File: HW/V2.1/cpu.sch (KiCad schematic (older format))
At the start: 74 parts, among them Q1 FDN360P, Q4 FDN360P, T2 TS-1136EVW, U1 STM32F302-SQ48, U2 MIC5501-3.0V, U3 BY25Q64ASSIG, U5 ESP8266EX, X1 TC2050-IDC, X3 TC2050-IDC

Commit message: updated values
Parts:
- removed F1: 120R@100MHz, Resistor_SMD:R_0805_2012Metric, symbol Device:Ferrite_Bead
- added FB2: Ferret, Inductor_SMD:L_0805_2012Metric, symbol Device:Ferrite_Bead
- C11, C15: value 4u7 16V -> 82n
- C8: value 10u 6,3V -> 1u 25V
- C9: value 22p 50V -> 18p 50V
- FB1: value Ferrite_Bead -> Ferret
- T2: value TS-1136EVW -> Panasonic_EVQPUL_EVQPUC
- U1: value STM32F302-SQ48 -> STM32F334
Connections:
- net 3V3: now also FB2.2
- net at C3.2, C4.2, U1.9 (VDDA/VREF+): now also FB2.1
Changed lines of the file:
@@
 P 9700 1900
 F 0 "C8" V 9803 1690 60  0000 R CNN
-F 1 "10u 6,3V" V 9697 1690 60  0000 R CNN
+F 1 "1u 25V" V 9697 1690 60  0000 R CNN
 F 2 "Capacitor_SMD:C_0603_1608Metric" H 9610 1710 60  0001 C CNN
 F 3 "" H 9610 1710 60  0000 C CNN
@@
 P 1950 7100
 F 0 "C15" H 2000 6837 60  0000 C CNN
-F 1 "4u7 16V" H 2000 6731 60  0000 C CNN
+F 1 "82n" H 2000 6731 60  0000 C CNN
 F 2 "Capacitor_SMD:C_0603_1608Metric" H 1940 6810 60  0001 C CNN
 F 3 "" H 1940 6810 60  0000 C CNN
@@
 P 1950 6700
 F 0 "C11" H 2000 6869 60  0000 C CNN
-F 1 "4u7 16V" H 2000 6763 60  0000 C CNN
+F 1 "82n" H 2000 6763 60  0000 C CNN
 F 2 "Capacitor_SMD:C_0603_1608Metric" H 1940 6410 60  0001 C CNN
 F 3 "" H 1940 6410 60  0000 C CNN
@@
 P 12750 4950
 F 0 "C9" H 12800 5119 60  0000 C CNN
-F 1 "22p 50V" H 12800 5013 60  0000 C CNN
+F 1 "18p 50V" H 12800 5013 60  0000 C CNN
 F 2 "Capacitor_SMD:C_0603_1608Metric" H 12740 4660 60  0001 C CNN
 F 3 "" H 12740 4660 60  0000 C CNN
@@
 P 15450 6100
 F 0 "T2" V 15397 5870 60  0000 R CNN
-F 1 "TS-1136EVW" V 15503 5870 60  0000 R CNN
+F 1 "Panasonic_EVQPUL_EVQPUC" V 15750 5750 60  0000 R CNN
 F 2 "Button_Switch_SMD:Panasonic_EVQPUL_EVQPUC" H 15440 6300 60  0001 C CNN
 F 3 "" H 15440 6300 60  0000 C CNN
@@
 Wire Wire Line
 	9800 1650 9800 1600
-$Comp
-L Device:Ferrite_Bead F1
-U 1 1 5D2B5837
-P 3100 1800
-F 0 "F1" V 2804 1800 60  0000 C CNN
-F 1 "120R@100MHz" V 2910 1800 60  0000 C CNN
-F 2 "Resistor_SMD:R_0805_2012Metric" V 2910 1800 60  0001 C CNN
-F 3 "" H 2700 1500 60  0000 C CNN
-	1    3100 1800
-	0    1    1    0
-$EndComp
 Wire Wire Line
 	2950 1800 2900 1800
@@
 P 4700 3700
 F 0 "U1" H 4700 6489 60  0000 C CNN
-F 1 "STM32F302-SQ48" H 4700 6383 60  0000 C CNN
+F 1 "STM32F334" H 4700 6383 60  0000 C CNN
 F 2 "Package_QFP:TQFP-48_7x7mm_P0.5mm" H 4100 4950 60  0001 C CNN
 F 3 "" H 4100 4950 60  0000 C CNN
@@
 P 7900 8600
 F 0 "FB1" H 8037 8646 50  0000 L CNN
-F 1 "Ferrite_Bead" H 8037 8555 50  0000 L CNN
+F 1 "Ferret" H 8037 8555 50  0000 L CNN
 F 2 "Inductor_SMD:L_0805_2012Metric" V 7830 8600 50  0001 C CNN
 F 3 "~" H 7900 8600 50  0001 C CNN
@@
 Connection ~ 7900 9400
 NoConn ~ 11450 5050
+$Comp
+L Device:Ferrite_Bead FB2
+U 1 1 5D49F431
+P 3100 1800
+F 0 "FB2" V 2826 1800 50  0000 C CNN
+F 1 "Ferret" V 2917 1800 50  0000 C CNN
+F 2 "Inductor_SMD:L_0805_2012Metric" V 3030 1800 50  0001 C CNN
+F 3 "~" H 3100 1800 50  0001 C CNN
+	1    3100 1800
+	0    1    1    0
+$EndComp
 $EndSCHEMATC

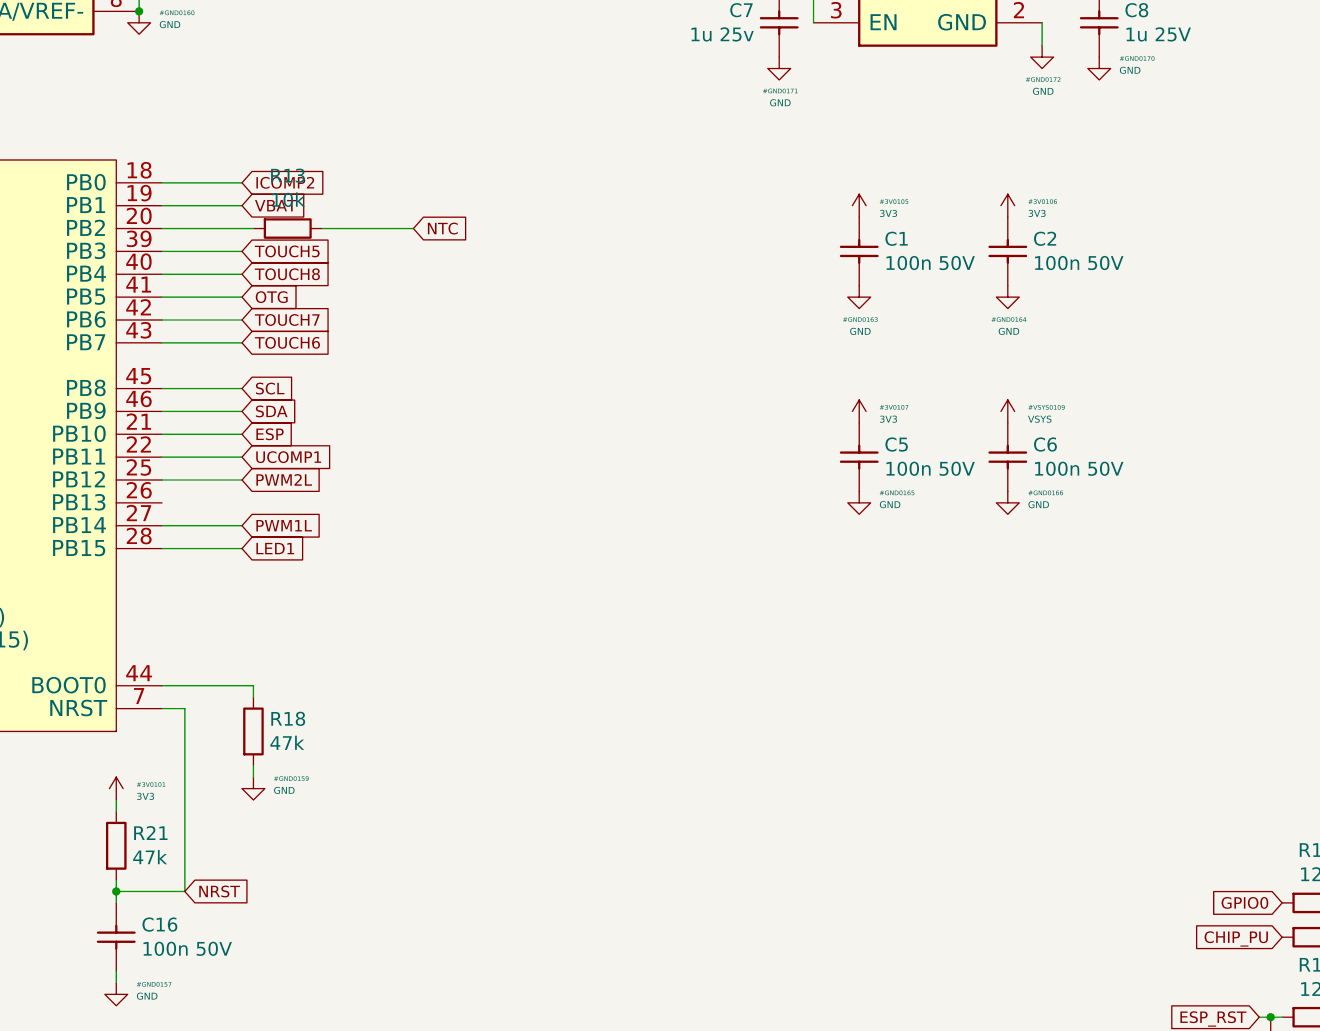
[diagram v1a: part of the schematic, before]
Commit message: added touch ic, fixed sk6812
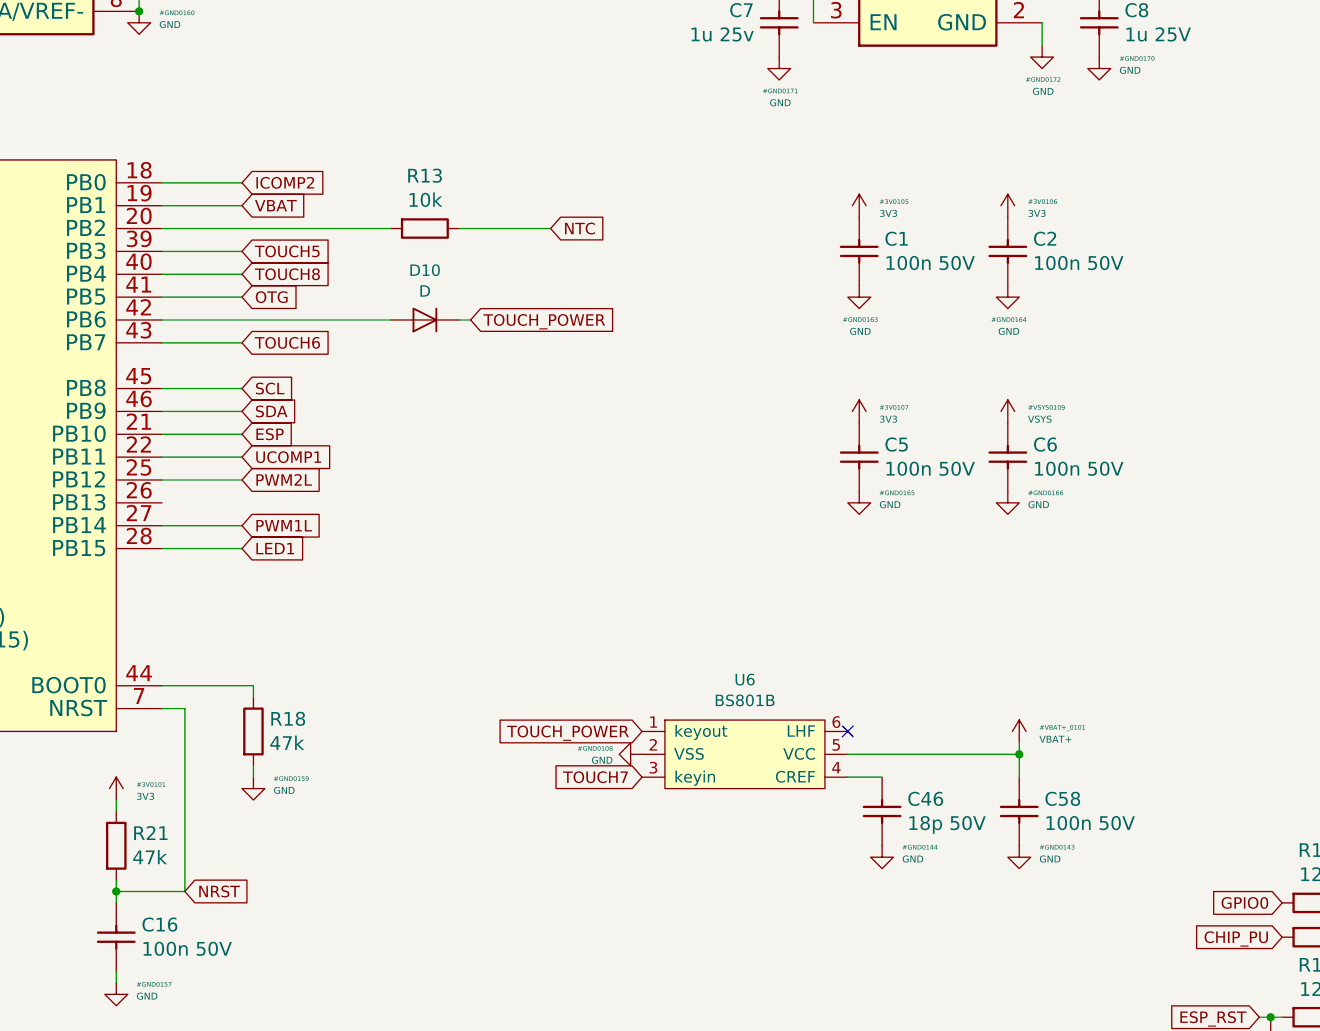
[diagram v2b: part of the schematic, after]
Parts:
- added C46: 18p 50V, Capacitor_SMD:C_0603_1608Metric, symbol EO:C-0402-18p-50V
- added C58: 100n 50V, Capacitor_SMD:C_0603_1608Metric, symbol EO:C-0603-100n-50V
- added D10: D, Diode_SMD:D_SOD-123F, symbol Device:D
- added U6: BS801B, Package_TO_SOT_SMD:SOT-23-6, symbol otter:BS801B
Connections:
- net GND: now also C46.1, C58.2, U6.2 (VSS)
- net TOUCH7: now also U6.3 (keyin); no longer U1.42 (PB6)
- new net: D10.2 (A), U1.42 (PB6)
- new net: C46.2, U6.4 (CREF)
- new net TOUCH_POWER: D10.1 (K), U6.1 (keyout)
- new net VBAT+: C58.1, U6.5 (VCC)
- no-connect marks 1 -> 2
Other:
- moved on the sheet: R13
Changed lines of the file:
@@
 L Device:R R13
 U 1 1 5D2B584B
-P 6250 2750
-F 0 "R13" V 6021 2750 60  0000 C CNN
-F 1 "10k" V 6127 2750 60  0000 C CNN
-F 2 "Resistor_SMD:R_0603_1608Metric" H 6250 2510 60  0001 C CNN
-F 3 "" H 6250 2510 60  0000 C CNN
-	1    6250 2750
+P 6850 2750
+F 0 "R13" V 6621 2750 60  0000 C CNN
+F 1 "10k" V 6727 2750 60  0000 C CNN
+F 2 "Resistor_SMD:R_0603_1608Metric" H 6850 2510 60  0001 C CNN
+F 3 "" H 6850 2510 60  0000 C CNN
+	1    6850 2750
 	0    1    1    0
 $EndComp
@@
 	6100 4800 6100 4750
 Wire Wire Line
-	6400 2750 6800 2750
+	7000 2750 7400 2750
 Connection ~ 8400 1650
 Wire Wire Line
@@
 	5700 2950 6050 2950
 Wire Wire Line
-	5700 3150 6050 3150
-Wire Wire Line
 	5700 3250 6050 3250
 Wire Wire Line
@@
 Wire Wire Line
 	3200 3150 3700 3150
-Wire Wire Line
-	5700 2750 6100 2750
 Wire Wire Line
 	3250 1800 3400 1800
@@
 Text GLabel 5800 5650 2    50   Input ~ 0
 NRST
-Text GLabel 6800 2750 2    50   Input ~ 0
+Text GLabel 7400 2750 2    50   Input ~ 0
 NTC
 Text GLabel 6050 2850 2    50   Input ~ 0
@@
 Text GLabel 6050 3050 2    50   Input ~ 0
 OTG
-Text GLabel 6050 3150 2    50   Input ~ 0
-TOUCH7
 Text GLabel 6050 2950 2    50   Input ~ 0
 TOUCH8
@@
 Text Label 3200 4050 0    60   ~ 0
 SWCLK
-Text GLabel 1350 5800 3    50   Input ~ 0
-NTC
 Text GLabel 1500 7200 0    50   Input ~ 0
 TOUCH5
@@
 	0    1    1    0
 $EndComp
+$Comp
+L otter:BS801B U6
+U 1 1 5D767019
+P 8250 5050
+F 0 "U6" H 8250 5375 50  0000 C CNN
+F 1 "BS801B" H 8250 5284 50  0000 C CNN
+F 2 "Package_TO_SOT_SMD:SOT-23-6" H 8250 5250 50  0001 C CNN
+F 3 "" H 8250 5250 50  0001 C CNN
+	1    8250 5050
+	1    0    0    -1
+$EndComp
+Text GLabel 7800 5150 0    50   Input ~ 0
+TOUCH7
+$Comp
+L power:GND #GND0108
+U 1 1 5D774B01
+P 7800 5050
+F 0 "#GND0108" V 7775 4923 20  0000 R CNN
+F 1 "GND" V 7827 4923 30  0000 R CNN
+F 2 "" H 7800 5050 70  0000 C CNN
+F 3 "" H 7800 5050 70  0000 C CNN
+	1    7800 5050
+	0    1    1    0
+$EndComp
+Text GLabel 7800 4950 0    50   Input ~ 0
+TOUCH_POWER
+NoConn ~ 8700 4950
+$Comp
+L EO:C-0603-100n-50V C58
+U 1 1 5D7A59D1
+P 9550 5250
+F 0 "C58" V 9547 5260 60  0000 L CNN
+F 1 "100n 50V" V 9653 5260 60  0000 L CNN
+F 2 "Capacitor_SMD:C_0603_1608Metric" H 9460 5060 60  0001 C CNN
+F 3 "" H 9460 5060 60  0000 C CNN
+	1    9550 5250
+	0    1    1    0
+$EndComp
+$Comp
+L power:GND #GND0143
+U 1 1 5D7A59D8
+P 9450 5450
+F 0 "#GND0143" H 9538 5443 20  0000 L CNN
+F 1 "GND" H 9538 5391 30  0000 L CNN
+F 2 "" H 9450 5450 70  0000 C CNN
+F 3 "" H 9450 5450 70  0000 C CNN
+	1    9450 5450
+	1    0    0    -1
+$EndComp
+Wire Wire Line
+	9450 5050 8700 5050
+$Comp
+L EO:C-0402-18p-50V C46
+U 1 1 5D7BEE89
+P 8750 5350
+F 0 "C46" V 8853 5140 60  0000 R CNN
+F 1 "18p 50V" V 8747 5140 60  0000 R CNN
+F 2 "Capacitor_SMD:C_0603_1608Metric" H 8860 5440 60  0001 C CNN
+F 3 "" H 8860 5440 60  0000 C CNN
+	1    8750 5350
+	0    -1   -1   0
+$EndComp
+Wire Wire Line
+	8700 5150 8850 5150
+$Comp
+L power:GND #GND0144
+U 1 1 5D7E35AF
+P 8850 5450
+F 0 "#GND0144" H 8938 5443 20  0000 L CNN
+F 1 "GND" H 8938 5391 30  0000 L CNN
+F 2 "" H 8850 5450 70  0000 C CNN
+F 3 "" H 8850 5450 70  0000 C CNN
+	1    8850 5450
+	1    0    0    -1
+$EndComp
+$Comp
+L EO:VBAT+ #VBAT+_?
+U 1 1 5D7F0297
+P 9450 5000
+AR Path="/5D7F0297" Ref="#VBAT+_?"  Part="1"
+AR Path="/5D2BD306/5D7F0297" Ref="#VBAT+_0101"  Part="1"
+F 0 "#VBAT+_0101" H 9538 5067 20  0000 L CNN
+F 1 "VBAT+" H 9538 5015 30  0000 L CNN
+F 2 "" H 9450 5000 70  0000 C CNN
+F 3 "" H 9450 5000 70  0000 C CNN
+	1    9450 5000
+	1    0    0    -1
+$EndComp
+Wire Wire Line
+	9450 5000 9450 5050
+Wire Wire Line
+	9450 5150 9450 5050
+Connection ~ 9450 5050
+$Comp
+L Device:D D?
+U 1 1 5D84EDDD
+P 6850 3150
+AR Path="/5D2BCF2C/5D84EDDD" Ref="D?"  Part="1"
+AR Path="/5D2BD306/5D84EDDD" Ref="D10"  Part="1"
+F 0 "D10" H 6850 2934 50  0000 C CNN
+F 1 "D" H 6850 3025 50  0000 C CNN
+F 2 "Diode_SMD:D_SOD-123F" H 6850 3150 50  0001 C CNN
+F 3 "~" H 6850 3150 50  0001 C CNN
+	1    6850 3150
+	-1   0    0    1
+$EndComp
+Text GLabel 7050 3150 2    50   Input ~ 0
+TOUCH_POWER
+Wire Wire Line
+	7050 3150 7000 3150
+Wire Wire Line
+	5700 2750 6700 2750
+Text GLabel 1350 5800 3    50   Input ~ 0
+NTC
+Wire Wire Line
+	5700 3150 6700 3150
 $EndSCHEMATC
